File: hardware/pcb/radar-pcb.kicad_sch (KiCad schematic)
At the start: 67 parts, among them J1 USB-C zasilanie 5 V (GCT USB4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, J10 Awaryjne wgrywanie: BOOT GND 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, J2 DevKit J1, J3 DevKit J3, J4 HC-SR04 (kabel): VCC TRIG ECH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, J5 Serwo SG90 (kabel): GND +5V S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, J6 MAX7219 Elegoo: VCC GND DIN C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, J7 OLED SH1106: VCC GND SCK SDA, J8 Buzzer: + -, J9 Przycisk zewnetrzny, Q2 MMBT3904, SW1 Przycisk ON/standby (katowy), U1 SN74AHCT125D, U2 AP22804AW5 (przelacznik 5 V, 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

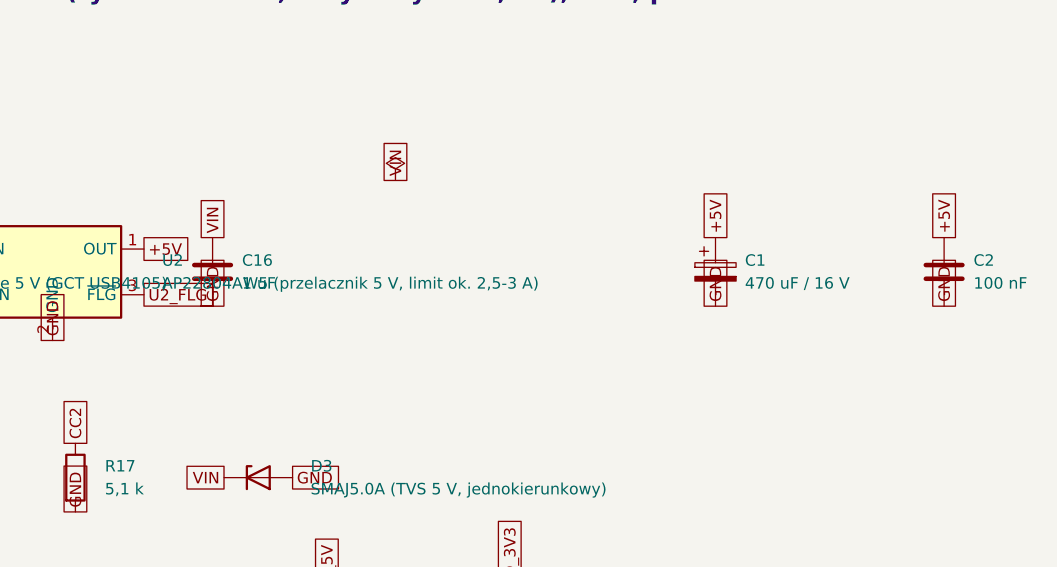
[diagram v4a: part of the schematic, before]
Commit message: PCB: napisy 1 mm (wymóg JLCPCB), U2 zmieniony na AP22802AW5-7 (C211404)
Wszystkie napisy na silkscreenie mają wysokość 1,0 mm i grubość 0,17 mm, obrysy
elementów min. 0,15 mm; opisy przeorganizowane (C14/C15/R22/R23/R24/R25 w legendzie,
ukryte oznaczenia otworów). Dodany tryb relabel w gen_pcb.py. U2 pin w pin zamiennik,
bo AP22804AW5 nie ma w katalogu JLCPCB. ERC 0 błędów, DRC 0 naruszeń, 0 niepołączonych,
0 niezgodności ze schematem. Nie sprawdzone na sprzęcie.

Co-Authored-By: Claude Sonnet 5.5 <noreply@anthropic.com>
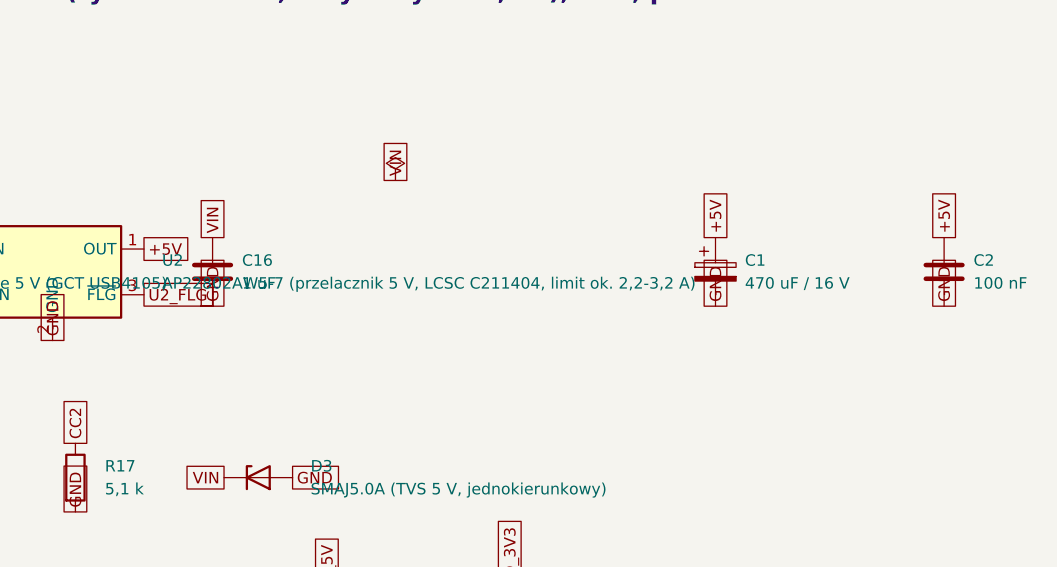
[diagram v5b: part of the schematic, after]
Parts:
- U2: value AP22804AW5 (przelacznik 5 V, limit ok. 2,5-3 A) -> AP22802AW5-7 (przelacznik 5 V, LCSC C211404, limit ok. 2,2-3,2 A)

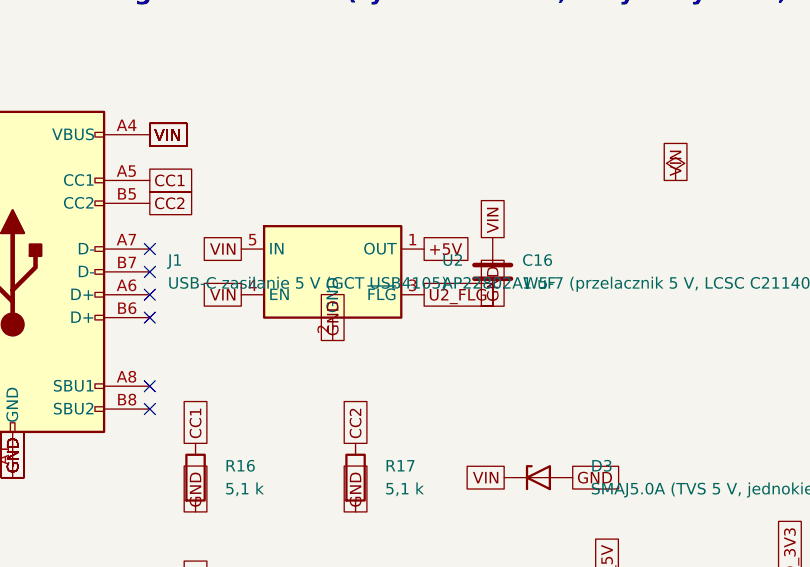
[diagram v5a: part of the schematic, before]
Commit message: PCB: USB-C zmienione na HRO TYPE-C-31-M-12 (LCSC C165948), BOM z C96346 dla 100 kΩ
GCT USB4105-GF-A był niedostępny w JLCPCB. Nowy footprint z biblioteki KiCad, gniazdo
przesunięte o 0,36 mm ku krawędzi (x = 2,74), usunięte dwa odcinki obrysu silkscreenu przy
krawędzi. Pełny build: ERC 0 błędów, DRC 0 błędów i 0 niepołączonych, 0 niezgodności ze
schematem, jedno ostrzeżenie lib_footprint_mismatch (celowa zmiana obrysu). Odświeżone rendery
i pliki produkcyjne. Nie sprawdzone na sprzęcie.

Co-Authored-By: Claude Sonnet 5.5 <noreply@anthropic.com>
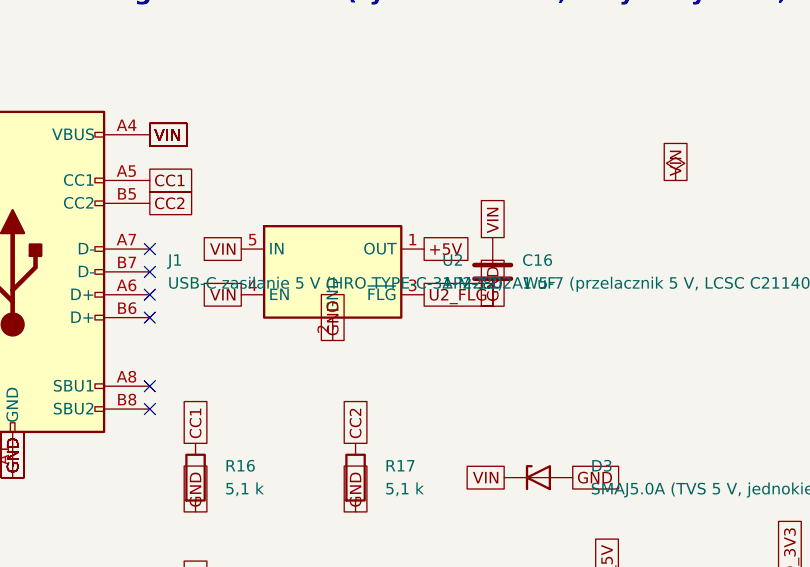
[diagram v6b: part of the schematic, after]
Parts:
- J1: value USB-C zasilanie 5 V (GCT USB4105) -> USB-C zasilanie 5 V (HRO TYPE-C-31-M-12); footprint Connector_USB:USB_C_Receptacle_GCT_USB4105-xx-A_16P_TopMnt_Horizontal -> Connector_USB:USB_C_Receptacle_HRO_TYPE-C-31-M-12

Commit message: PCB v0.2: wersja przewlekana (gniazdo DC, PTC + TVS, DIP-14), piny DevKita na listwach, pole prototypowe; firmware bez CC/FLG
Wszystko do ręcznego lutowania, płytki zamawiane bez montażu. Rozmieszczenie automatyczne
(tools/autoplace.py, geom.py), płytka 76 x 137,5 mm. J11/J12 = kopie wszystkich pinów DevKita,
J13 = listwa GND/3V3/5V, 4 bloki 2x14 = pole prototypowe. Miejsce na logo (footprint z Image Convertera)
w prawym dolnym rogu. POWER_MONITOR_USB_C=0 w firmware (tylko pomiar 5 V). Lista zakupów i Gerbery
w production/. ERC 0 błędów; DRC 0 błędów, 0 niepołączonych, 0 niezgodności ze schematem
(5 ostrzeżeń lib_footprint_mismatch: celowo uproszczone J1 i J14-J17). pio run przechodzi.
Nic nie sprawdzono na sprzęcie.

Co-Authored-By: Claude Sonnet 5.5 <noreply@anthropic.com>
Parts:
- removed C14, C15: 100 nF, Capacitor_SMD:C_0805_2012Metric, symbol Device:C
- removed C16: 1 uF, Capacitor_SMD:C_0805_2012Metric, symbol Device:C
- removed FB1: 0 R (zworka; opcja: ferryt >= 1 A), Inductor_SMD:L_0805_2012Metric, symbol Device:FerriteBead
- removed J1: USB-C zasilanie 5 V (HRO TYPE-C-31-M-12), Connector_USB:USB_C_Receptacle_HRO_TYPE-C-31-M-12, symbol Connector:USB_C_Receptacle_USB2.0_16P
- removed Q2: MMBT3904, Package_TO_SOT_SMD:SOT-23, symbol Transistor_BJT:MMBT3904
- removed R16, R17: 5,1 k, Resistor_SMD:R_0805_2012Metric, symbol Device:R
- removed R22, R23: 100 k, Resistor_SMD:R_0805_2012Metric, symbol Device:R
- removed R26: 10 k, Resistor_SMD:R_0805_2012Metric, symbol Device:R
- removed U2: AP22802AW5-7 (przelacznik 5 V, LCSC C211404, limi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, Package_TO_SOT_SMD:SOT-23-5, symbol Power_Management:AP22804AW5
- added F1: PTC 2 A (hold), rastr 5 mm, Capacitor_THT:C_Disc_D7.5mm_W5.0mm_P5.00mm, symbol Device:Polyfuse
- added FB1: 0 R (zworka z drutu; opcja: ferryt >= 1 A), Resistor_THT:R_Axial_DIN0207_L6.3mm_D2.5mm_P7.62mm_Horizontal, symbol Device:R
- added J1: Gniazdo DC 5,5/2,1 mm, srodek +5 V, Connector_BarrelJack:BarrelJack_Horizontal, symbol Connector:Barrel_Jack_Switch
- added J11: Piny DevKit J3 (kopia J3), Connector_PinHeader_2.54mm:PinHeader_1x16_P2.54mm_Vertical, symbol Connector_Generic:Conn_01x16
- added J12: Piny DevKit J1 (kopia J2), Connector_PinHeader_2.54mm:PinHeader_1x16_P2.54mm_Vertical, symbol Connector_Generic:Conn_01x16
- added J13: Listwa zasilania: GND 3V3 5V, Connector_PinHeader_2.54mm:PinHeader_1x08_P2.54mm_Vertical, symbol Connector_Generic:Conn_01x08
- added J14: Pole prototypowe 1 (2x14, niepodlaczone), Connector_PinHeader_2.54mm:PinHeader_2x14_P2.54mm_Vertical, symbol Connector_Generic:Conn_02x14_Odd_Even
- added J15: Pole prototypowe 2 (2x14, niepodlaczone), Connector_PinHeader_2.54mm:PinHeader_2x14_P2.54mm_Vertical, symbol Connector_Generic:Conn_02x14_Odd_Even
- added J16: Pole prototypowe 3 (2x14, niepodlaczone), Connector_PinHeader_2.54mm:PinHeader_2x14_P2.54mm_Vertical, symbol Connector_Generic:Conn_02x14_Odd_Even
- added J17: Pole prototypowe 4 (2x14, niepodlaczone), Connector_PinHeader_2.54mm:PinHeader_2x14_P2.54mm_Vertical, symbol Connector_Generic:Conn_02x14_Odd_Even
- added Q2: 2N3904 (TO-92, E B C), Package_TO_SOT_THT:TO-92_Inline, symbol Transistor_BJT:2N3904
- C10, C11, C12, C13, C2, C3, C5, C7, C9: footprint Capacitor_SMD:C_0805_2012Metric -> Capacitor_THT:C_Disc_D5.0mm_W2.5mm_P5.00mm
- D1: value LED zasilania -> LED zasilania 3 mm; footprint LED_SMD:LED_0805_2012Metric -> LED_THT:LED_D3.0mm
- D2: value 1N4148W -> 1N4148; footprint Diode_SMD:D_SOD-123 -> Diode_THT:D_DO-35_SOD27_P7.62mm_Horizontal
- D3: value SMAJ5.0A (TVS 5 V, jednokierunkowy) -> TVS SA5.0A (DO-15, katoda do +5V); footprint Diode_SMD:D_SMA -> Diode_THT:D_DO-15_P10.16mm_Horizontal
- D4: value 1N5819HW -> 1N5819; footprint Diode_SMD:D_SOD-123 -> Diode_THT:D_DO-41_SOD81_P10.16mm_Horizontal
- R1, R10, R11, R12, R13, R14, R15, R18, R19, R2, R20, R21, R24, R25, R3, R4, R5, R6, R7, R8, R9: footprint Resistor_SMD:R_0805_2012Metric -> Resistor_THT:R_Axial_DIN0207_L6.3mm_D2.5mm_P7.62mm_Horizontal
- TP1, TP2, TP3, TP4, TP5, TP6: footprint TestPoint:TestPoint_Pad_D1.5mm -> TestPoint:TestPoint_THTPad_D2.0mm_Drill1.0mm
- U1: value SN74AHCT125D -> SN74AHCT125N (DIP-14); footprint Package_SO:SOIC-14_3.9x8.7mm_P1.27mm -> Package_DIP:DIP-14_W7.62mm_Socket
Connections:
- net +3V3: now also J12.1 (Pin_1), J13.2 (Pin_2), J13.6 (Pin_6)
- net +5V: now also D3.1 (K), F1.2, FB1.1, J12.14 (Pin_14), J13.3 (Pin_3), J13.7 (Pin_7)
- net BOOT: now also J11.11 (Pin_11)
- net BTN_ESP: now also J12.12 (Pin_12)
- net BUZ_BASE: now also Q2.2 (B)
- net BUZ_CTRL: now also J11.6 (Pin_6)
- net BUZ_NEG: now also Q2.3 (C)
- net CLK_3V3: now also J11.10 (Pin_10)
- net CS_3V3: now also J11.9 (Pin_9)
- net DIN_3V3: now also J12.6 (Pin_6)
- net ECHO_3V3: now also J12.5 (Pin_5)
- net EN: now also J12.2 (Pin_2)
- net GND: now also J1.2, J11.1 (Pin_1), J11.12 (Pin_12), J11.15 (Pin_15), J12.15 (Pin_15), J13.1 (Pin_1), J13.4 (Pin_4), J13.5 (Pin_5), J13.8 (Pin_8), Q2.1 (E)
- net SCL: now also J11.7 (Pin_7)
- net SDA: now also J11.8 (Pin_8)
- net SERVO_3V3: now also J12.10 (Pin_10)
- net SERVO_5V: now also FB1.2
- net TRIG_3V3: now also J12.11 (Pin_11)
- net V5_SENSE: now also J12.7 (Pin_7)
- net VIN: now also F1.1, J1.1; no longer D3.1 (K)
- net IO13: now reaches J3.13 (Pin_13)
- net IO13: now also J11.13 (Pin_13)
- net IO12: now reaches J3.14 (Pin_14)
- net IO12: now also J11.14 (Pin_14)
- net TX: now reaches J3.2 (Pin_2)
- net TX: now also J11.2 (Pin_2)
- net RX: now reaches J3.3 (Pin_3)
- net RX: now also J11.3 (Pin_3)
- net IO15: now reaches J3.4 (Pin_4)
- net IO15: now also J11.4 (Pin_4)
- net IO4: now reaches J2.3 (Pin_3)
- net IO4: now also J12.3 (Pin_3)
- net IO5: now reaches J2.4 (Pin_4)
- net IO5: now also J12.4 (Pin_4)
- net IO8: now reaches J2.9 (Pin_9)
- net IO8: now also J12.9 (Pin_9)
- net CC1_SENSE renamed IO1
- net IO1: now also J12.8 (Pin_8)
- net CC2_SENSE renamed IO3
- net IO3: now also J12.13 (Pin_13)
- net U2_FLG renamed IO23
- net IO23: now also J11.5 (Pin_5)
- no-connect marks 16 -> 117
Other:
- note added: "BUFOR SN74AHCT125N (DIP-14 w podstawce): 3,3 V z ESP32 -> 5 V; wejscia A z pull-downami"
- note added: "BUZZER (aktywny lub pasywny, 5 V): tranzystor 2N3904 + dioda"
- note added: "DODATKI: dioda 5V DevKita, pomiar napiecia 5 V (ADC), BOOT/RST, pull-upy I2C (opcja), listwa zasilania, pole prototypowe"
- note added: "ESP32-C6-DevKitC-1 (gniazda zenskie 1x16). Wszystkie piny sa wyprowadzone na listwy J11 (lustro J3) i J12 (lustro J2). Pin 5V DevKita zasilany z +5V przez D4."
- note added: "ZASILANIE 5 V: gniazdo DC 5,5/2,1 mm (srodek +), bezpiecznik PTC i dioda TVS (zwiera przy przepieciu i odwroconej polaryzacji, PTC odcina)"
- note removed: "BUFOR SN74AHCT125 (DIP-14 w podstawce): 3,3 V z ESP32 -> 5 V; wejscia A z pull-downami"
- note removed: "BUZZER (typ do ustalenia): tranzystor + dioda"
- note removed: "DODATKI: dioda 5V DevKita, pomiary ADC (5V, CC1, CC2), BOOT/RST, pull-upy I2C (opcja)"
- note removed: "ESP32-C6-DevKitC-1 (gniazda zenskie 1x16, J1 i J3 DevKita). Pin 5V DevKita (J2 pin 14) zasilany z +5V przez diode Schottky D4 (kierunek plytka -> DevKit): USB DevKita nie zasila plytki."
- note removed: "ZASILANIE 5 V: gniazdo USB-C (tylko zasilanie, rezystory CC 5,1 k), TVS, przelacznik z miekkim startem"
- title: Radar sonarowy ESP32-C6 - plytka glowna -> Radar sonarowy ESP32-C6 - plytka glowna, wersja przewlekana
